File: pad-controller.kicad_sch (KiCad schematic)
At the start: 21 parts, among them J1 Conn_01x02, J3 Conn_01x02, J6 Conn_01x06, M1 Motor_Servo, M2 Motor_Servo, M3 Motor_Servo, M4 Motor_Servo, Q1 IRFP450PBF, Q2 IRFP450PBF, SW1 SW_Push_Dual, U1 Xbee

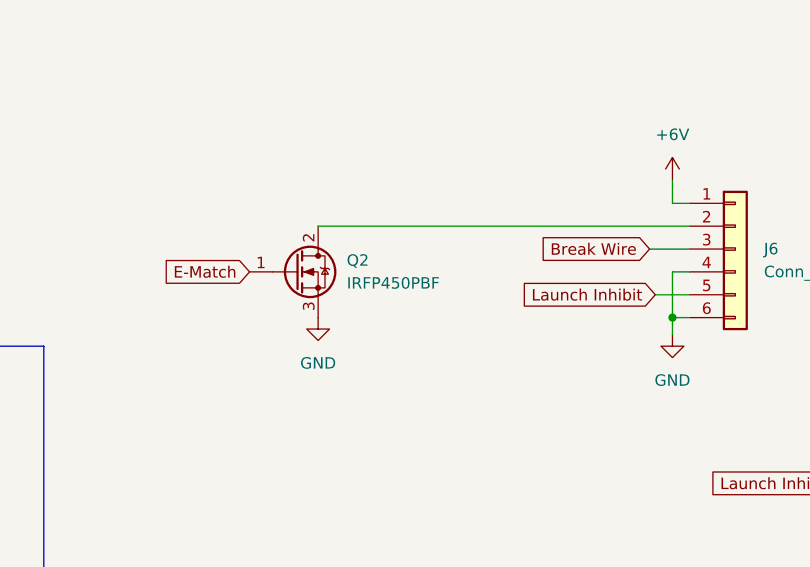
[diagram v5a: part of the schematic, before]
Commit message: Replace ignitor mosfet with FQP30N06L
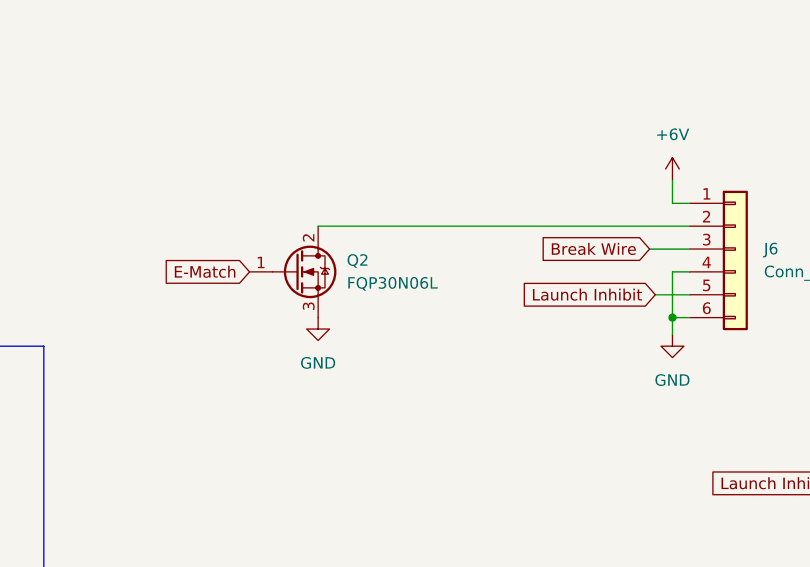
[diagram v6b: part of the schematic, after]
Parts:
- Q2: value IRFP450PBF -> FQP30N06L; footprint Package_TO_SOT_THT:TO-247-3_Vertical -> Package_TO_SOT_THT:TO-220-3_Vertical; Part No. IRFP450PBF -> FQP30N06L
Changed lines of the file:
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@@
       (effects (font (size 1.27 1.27)) (justify left))
     )
-    (property "Value" "IRFP450PBF" (at 158.115 118.11 0)
+    (property "Value" "FQP30N06L" (at 158.115 118.11 0)
       (effects (font (size 1.27 1.27)) (justify left))
     )
-    (property "Footprint" "Package_TO_SOT_THT:TO-247-3_Vertical" (at 157.48 114.3 0)
+    (property "Footprint" "Package_TO_SOT_THT:TO-220-3_Vertical" (at 157.48 114.3 0)
       (effects (font (size 1.27 1.27)) hide)
     )
-    (property "Datasheet" "https://www.vishay.com/docs/91233/91233.pdf" (at 152.4 116.84 0)
+    (property "Datasheet" "https://www.onsemi.com/pdf/datasheet/fqp30n06l-d.pdf" (at 152.4 116.84 0)
       (effects (font (size 1.27 1.27)) hide)
     )
-    (property "Part No." "IRFP450PBF" (at 152.4 116.84 0)
+    (property "Part No." "FQP30N06L" (at 152.4 116.84 0)
       (effects (font (size 1.27 1.27)) hide)
     )

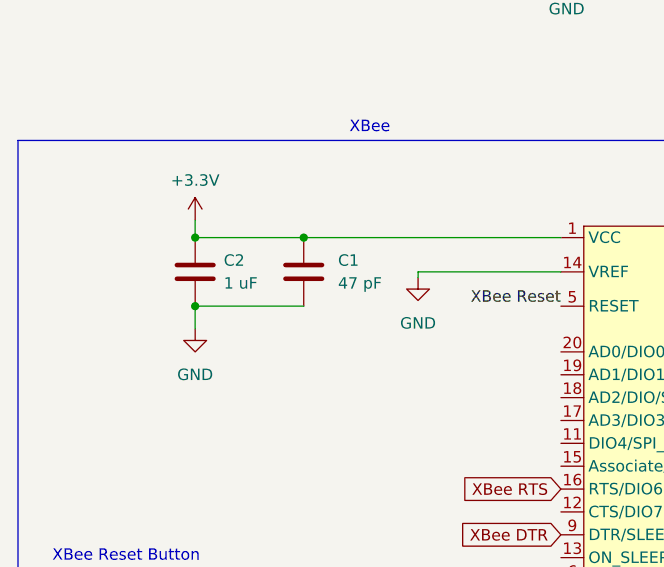
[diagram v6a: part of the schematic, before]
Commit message: Add part numbers for all capacitors
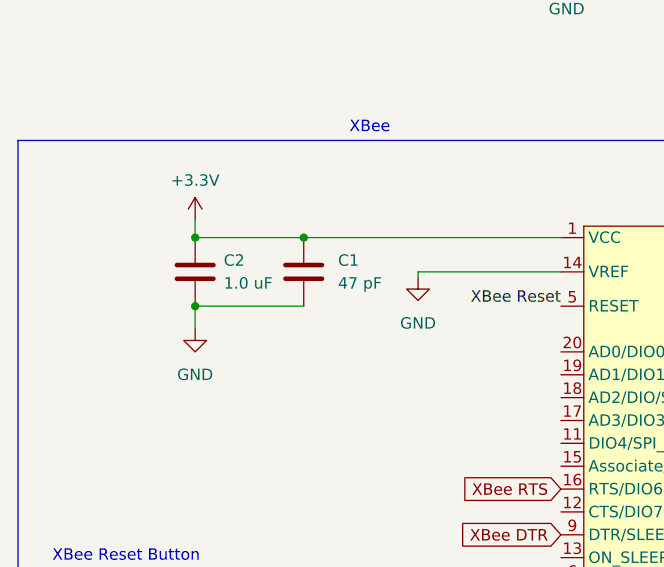
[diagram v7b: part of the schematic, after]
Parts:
- C1: Part No. (none) -> GRM21A5C2D470JW01D
- C2: value 1 uF -> 1.0 uF; Part No. (none) -> GRM219R7YA105MA12D
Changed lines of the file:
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@@
       (effects (font (size 1.27 1.27)) (justify left))
     )
-    (property "Value" "1 uF" (at 40.64 140.97 0)
+    (property "Value" "1.0 uF" (at 40.64 140.97 0)
       (effects (font (size 1.27 1.27)) (justify left))
     )
@@
       (effects (font (size 1.27 1.27)) hide)
     )
-    (property "Part No." "" (at 37.465 139.7 0)
+    (property "Part No." "GRM219R7YA105MA12D" (at 37.465 139.7 0)
       (effects (font (size 1.27 1.27)) hide)
     )
@@
       (effects (font (size 1.27 1.27)) hide)
     )
-    (property "Part No." "" (at 49.53 139.7 0)
-      (effects (font (size 1.27 1.27)) hide)
-    )
+    (property "Part No." "GRM21A5C2D470JW01D" (at 49.53 139.7 0)
+      (effects (font (size 1.27 1.27)) hide)
+    )

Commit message: Adjust layout
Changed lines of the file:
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@@
     )
   )
-  (global_label "XBee RTS" (shape input) (at 45.72 51.435 180) (fields_autoplaced)
+  (global_label "XBee RTS" (shape input) (at 64.135 52.705 180) (fields_autoplaced)
     (effects (font (size 1.27 1.27)) (justify right))
-    (property "Intersheetrefs" "${INTERSHEET_REFS}" (at 33.6634 51.435 0)
+    (property "Intersheetrefs" "${INTERSHEET_REFS}" (at 52.0784 52.705 0)
       (effects (font (size 1.27 1.27)) (justify right) hide)
     )
@@
     )
   )
-  (global_label "XBee DTR" (shape input) (at 45.72 53.975 180) (fields_autoplaced)
+  (global_label "XBee DTR" (shape input) (at 64.135 55.245 180) (fields_autoplaced)
     (effects (font (size 1.27 1.27)) (justify right))
-    (property "Intersheetrefs" "${INTERSHEET_REFS}" (at 33.6029 53.975 0)
+    (property "Intersheetrefs" "${INTERSHEET_REFS}" (at 52.0179 55.245 0)
       (effects (font (size 1.27 1.27)) (justify right) hide)
     )
